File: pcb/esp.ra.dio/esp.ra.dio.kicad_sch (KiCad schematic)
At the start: 26 parts, among them J1 A, J10 UART, J2 B, J3 C, J4 D, J5 START, J6 SELECT, J7 JOY, J8 USB_B_Micro, J9 BATTERY, SW1 RESET, SW2 POWER, SW3 BOOT, U2 VCC, U3 TLV75533PDBV

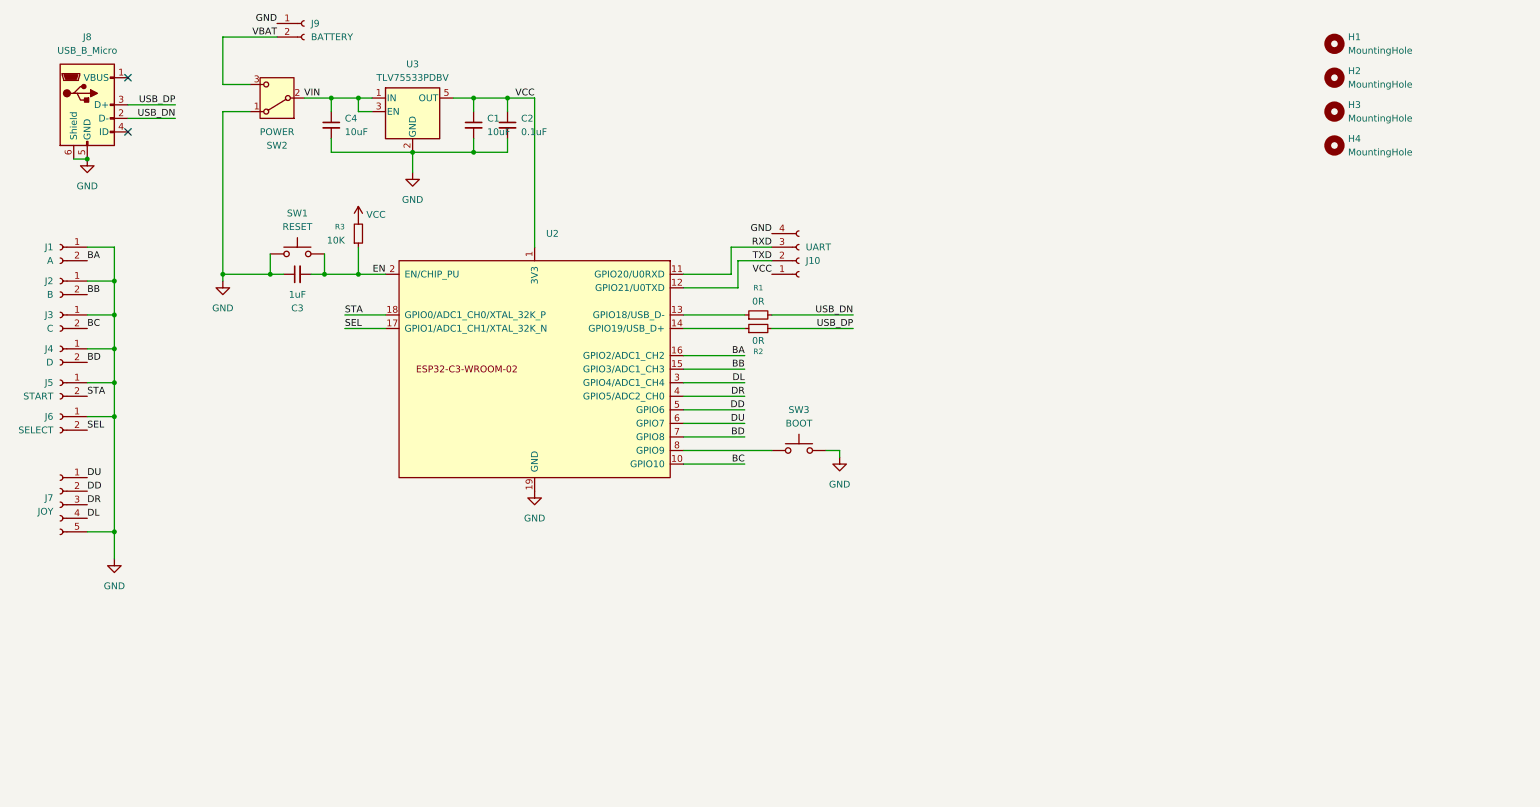
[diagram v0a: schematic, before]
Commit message: Add activity LED, add weak pullups to strapping pins 2 and 8
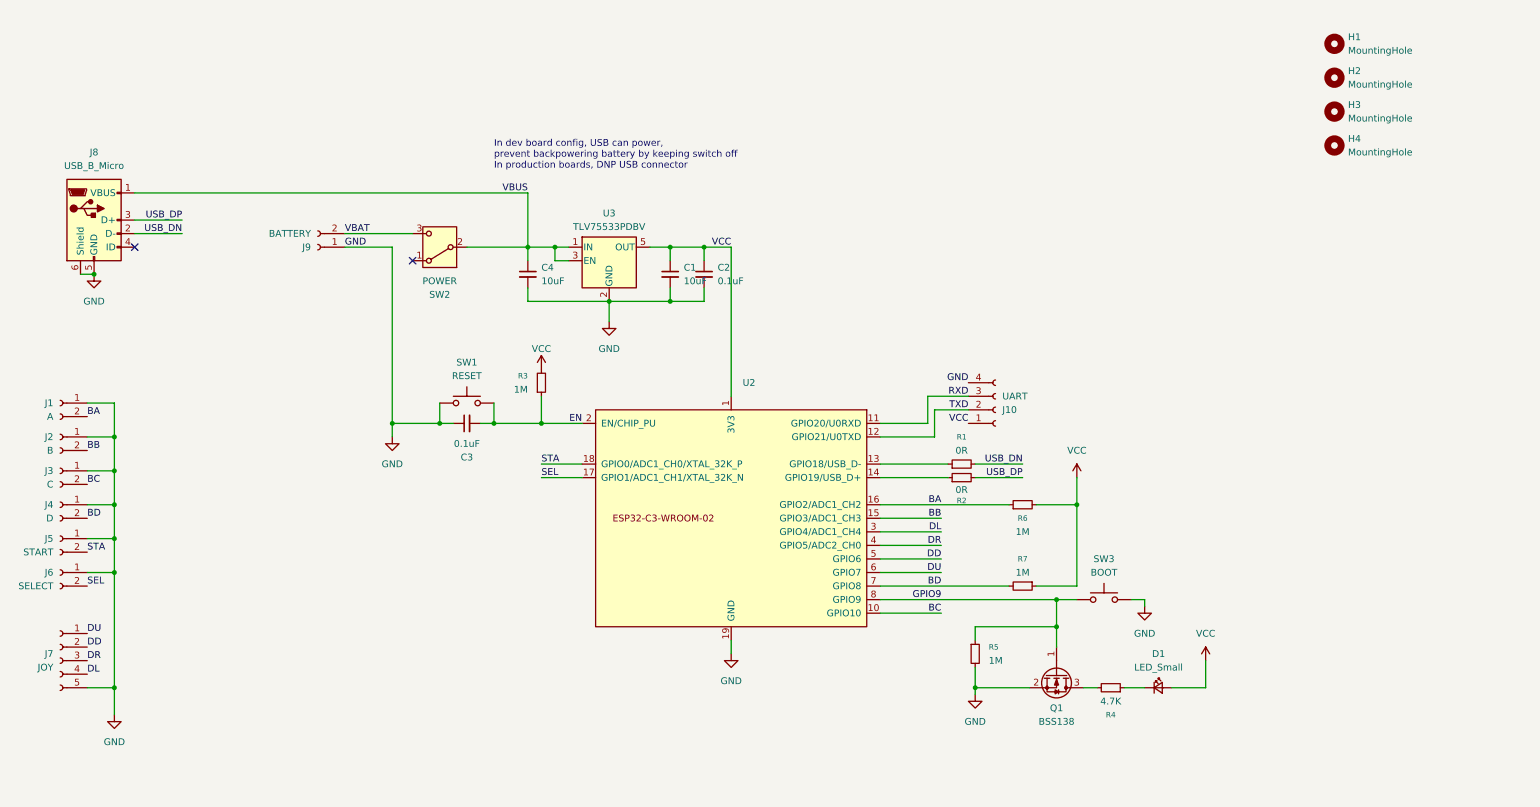
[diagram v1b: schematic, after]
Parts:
- added D1: LED_Small, LED_THT:LED_D3.0mm_Horizontal_O1.27mm_Z6.0mm, symbol Device:LED_Small
- added Q1: BSS138, Package_TO_SOT_SMD:SOT-23, symbol Transistor_FET:BSS138
- added R4: 4.7K, Resistor_SMD:R_0805_2012Metric_Pad1.20x1.40mm_HandSolder, symbol Device:R_Small
- added R5, R6, R7: 1M, Resistor_SMD:R_0805_2012Metric_Pad1.20x1.40mm_HandSolder, symbol Device:R_Small
- C3: value 1uF -> 0.1uF
- R3: value 10K -> 1M
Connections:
- net VIN is gone; now on net VBUS: C4.1, SW2.2 (B), U3.1 (IN), U3.3 (EN)
- net BA: now also R6.1
- net BD: now also R7.2
- net GND: now also Q1.2 (S), R5.2; no longer SW2.1 (A)
- net VCC: now also D1.2 (A), R6.2, R7.1
- net GPIO9: now reaches SW3.1, U2.8 (GPIO9)
- net GPIO9: now also Q1.1 (G), R5.1
- net VBUS: now reaches J8.1 (VBUS)
- new net: D1.1 (K), R4.1
- new net: Q1.3 (D), R4.2
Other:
- note added: "In dev board config, USB can power, prevent backpowering battery by keeping switch off In production boards, DNP USB connector"
- moved on the sheet: C1, C2, C3, C4, J1, J10, J2, J3, J4, J5, J6, J7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

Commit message: Comments and cleanup of routing
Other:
- note removed: "In dev board config, USB can power, prevent backpowering battery by keeping switch off In production boards, DNP USB connector"
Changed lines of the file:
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@@
 		(company "@partlyhuman")
 	)
-	(text "In dev board config, USB can power,\nprevent backpowering battery by keeping switch off\nIn production boards, DNP USB connector"
+	(text_box "USB, RESET, BOOT buttons for development only, can DNP"
 		(exclude_from_sim no)
-		(at 107.95 41.148 0)
+		(at 27.94 30.48 0)
+		(size 26.67 7.62)
+		(margins 0.9525 0.9525 0.9525 0.9525)
+		(stroke
+			(width 0)
+			(type solid)
+		)
+		(fill
+			(type none)
+		)
 		(effects
 			(font
 				(size 1.27 1.27)
 			)
-			(justify left)
+			(justify left top)
 		)
 	)
+	(text_box "GPIO2, GPIO8, GPIO9 used in strapping\nGPIO2, GPIO8 float. GPIO9 has weak int. pullup\nJoint download mode requires\nGPIO2=1 GPIO8=1 GPIO9=0\nR6,R7 pullup GPIO2,8 always\nButton sinks GPIO9 to 0 for boot\nWeak pullups only help the pins' normal common GND button behaviour"
+		(exclude_from_sim no)
+		(at 222.25 91.44 0)
+		(size 50.8 17.78)
+		(margins 0.9525 0.9525 0.9525 0.9525)
+		(stroke
+			(width 0)
+			(type solid)
+		)
+		(fill
+			(type none)
+		)
+		(effects
+			(font
+				(size 1.27 1.27)
+			)
+			(justify left top)
+		)
+	)
+	(text_box "In dev board config, USB can power.\nEngineer must prevent backpowering batt by keeping switch off."
+		(exclude_from_sim no)
+		(at 74.93 30.48 0)
+		(size 39.37 7.62)
+		(margins 0.9525 0.9525 0.9525 0.9525)
+		(stroke
+			(width 0)
+			(type solid)
+		)
+		(fill
+			(type none)
+		)
+		(effects
+			(font
+				(size 1.27 1.27)
+			)
+			(justify left top)
+		)
+	)
+	(text_box "GPIO9 used for LED signalling in production.\nUsing low-side switch to avoid any current leakage.\nShould not interfere with bootstrapping behaviour, normally float with internal pullup to high = normal boot"
+		(exclude_from_sim no)
+		(at 196.85 151.13 0)
+		(size 59.69 10.16)
+		(margins 0.9525 0.9525 0.9525 0.9525)
+		(stroke
+			(width 0)
+			(type solid)
+		)
+		(fill
+			(type none)
+		)
+		(effects
+			(font
+				(size 1.27 1.27)
+			)
+			(justify left top)
+		)
+	)
+	(text_box "UART for programming production units"
+		(exclude_from_sim no)
+		(at 191.77 71.12 0)
+		(size 20.32 7.62)
+		(margins 0.9525 0.9525 0.9525 0.9525)
+		(stroke
+			(width 0)
+			(type solid)
+		)
+		(fill
+			(type none)
+		)
+		(effects
+			(font
+				(size 1.27 1.27)
+			)
+			(justify left top)
+		)
+	)

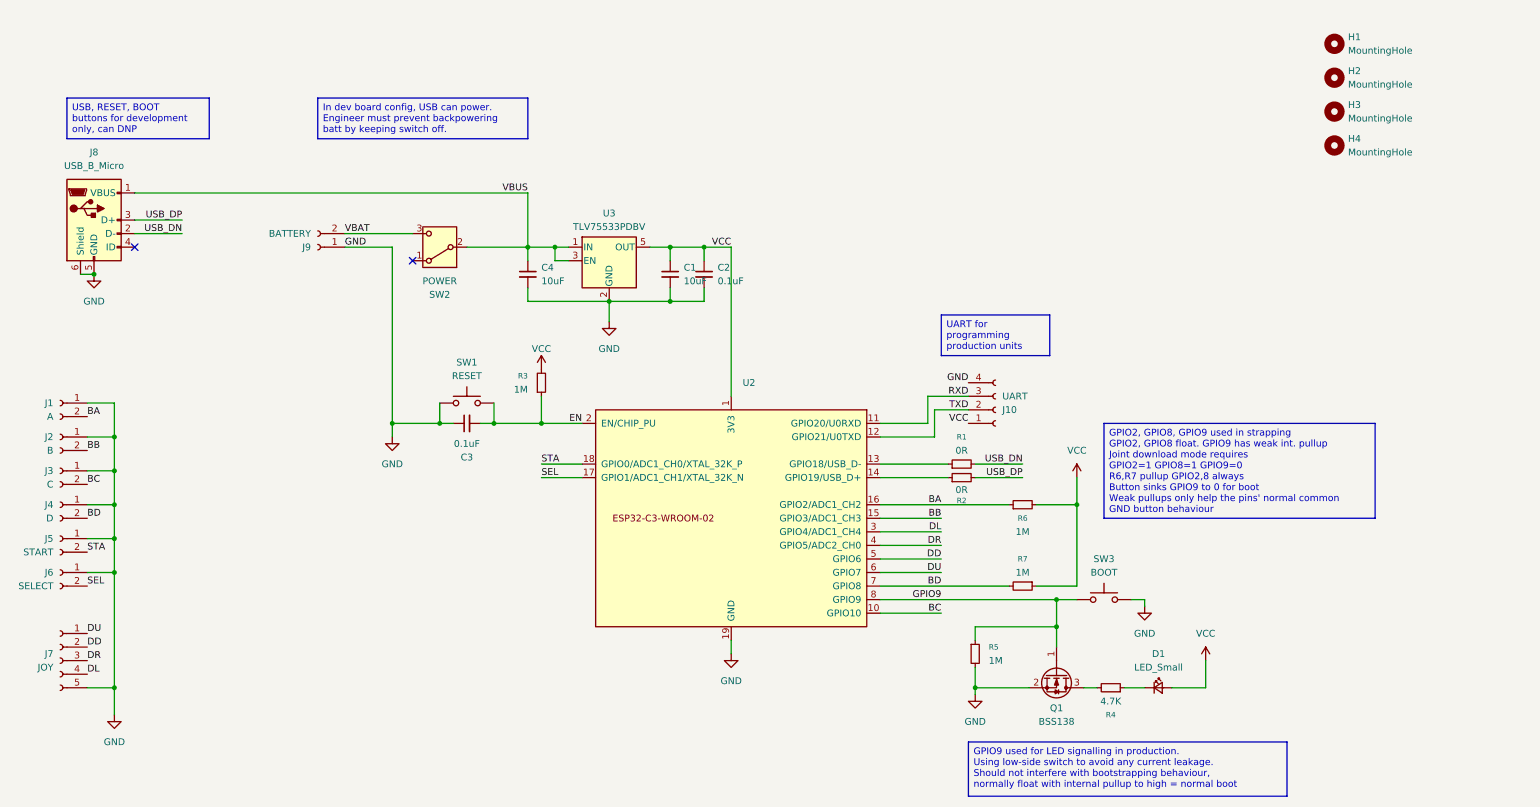
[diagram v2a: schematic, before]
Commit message: Fix strapping pins, move buttons doubling with strapping pins to TX/RX
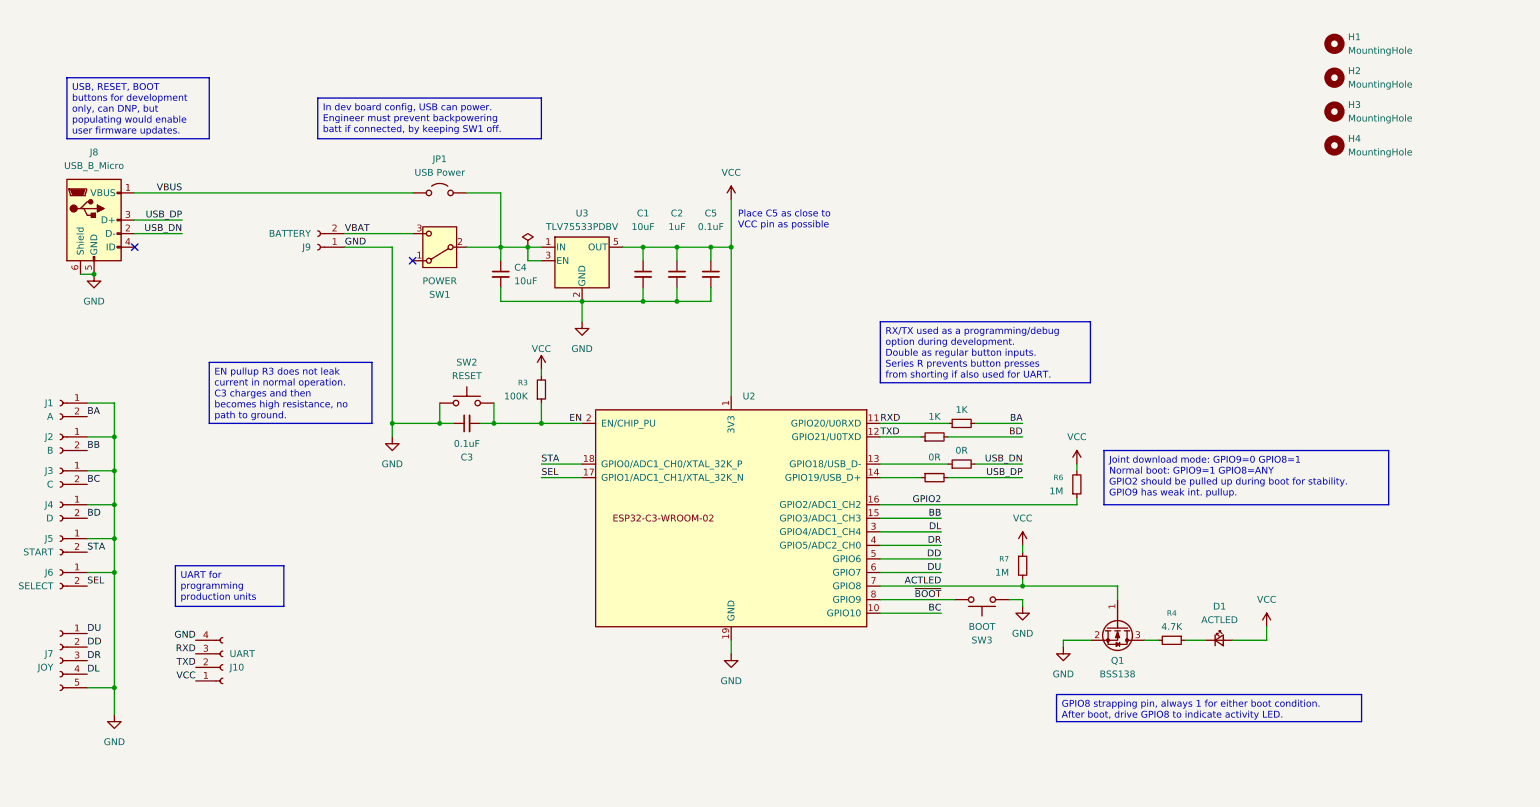
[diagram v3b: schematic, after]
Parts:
- removed R5: 1M, Resistor_SMD:R_0805_2012Metric_Pad1.20x1.40mm_HandSolder, symbol Device:R_Small
- added C5: 0.1uF, Capacitor_SMD:C_0805_2012Metric_Pad1.18x1.45mm_HandSolder, symbol Device:C_Small
- added JP1: USB Power, Connector_PinHeader_2.54mm:PinHeader_1x02_P2.54mm_Vertical, symbol Jumper:Jumper_2_Open
- added R8, R9: 1K, Resistor_SMD:R_0805_2012Metric_Pad1.20x1.40mm_HandSolder, symbol Device:R_Small
- C2: value 0.1uF -> 1uF
- D1: value LED_Small -> ACTLED
- R3: value 1M -> 100K
- renumbered SW2 to SW1, SW1 to SW2
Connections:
- net BA: now also R8.2; no longer R6.1, U2.16 (GPIO2/ADC1_CH2)
- net BD: now also R9.2; no longer R7.2, U2.7 (GPIO8)
- net GND: now also C5.2
- net RXD: now also R8.1
- net TXD: now also R9.1
- net VBUS: now also JP1.1 (A); no longer C4.1, SW1.2 (B), U3.1 (IN), U3.3 (EN)
- net VCC: now also C5.1
- net GPIO9 renamed ~{BOOT}
- net ~{BOOT}: no longer Q1.1 (G)
- new net: C4.1, JP1.2 (B), SW1.2 (B), U3.1 (IN), U3.3 (EN)
- new net ACTLED: Q1.1 (G), R7.2, U2.7 (GPIO8)
- new net GPIO2: R6.1, U2.16 (GPIO2/ADC1_CH2)
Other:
- note added: "Place C5 as close to VCC pin as possible"
- moved on the sheet: C1, C2, C4, D1, J10, Q1, R3, R4, R6, R7, SW3, U3

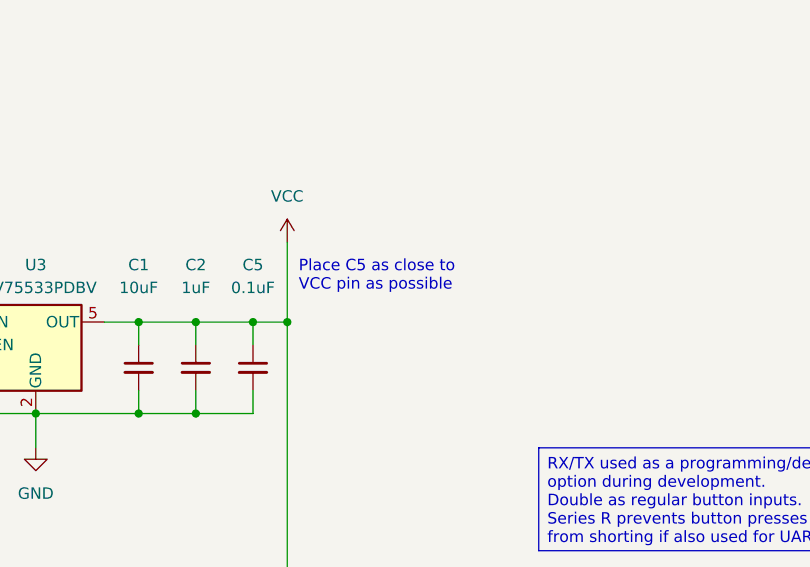
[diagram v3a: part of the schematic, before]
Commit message: oops backwards text
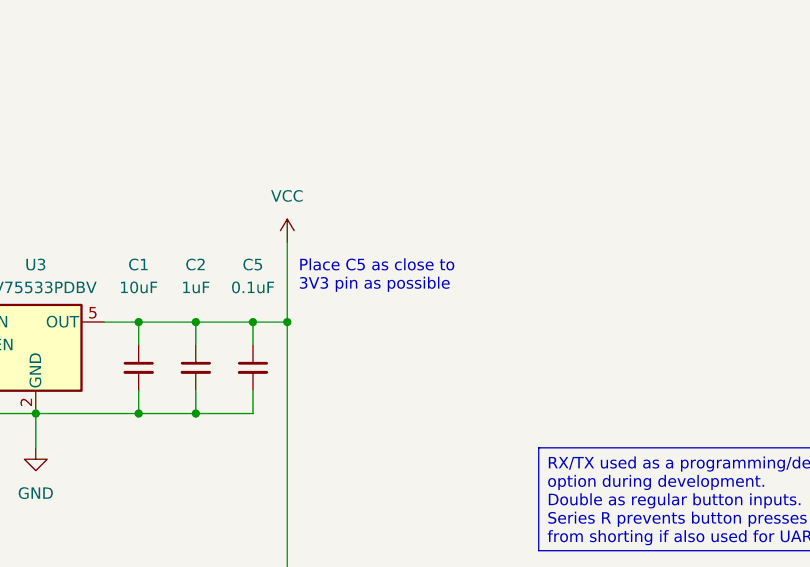
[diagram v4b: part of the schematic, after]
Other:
- note added: "Place C5 as close to 3V3 pin as possible"
- note removed: "Place C5 as close to VCC pin as possible"
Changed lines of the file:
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@@
 		(company "@partlyhuman")
 	)
-	(text "Place C5 as close to\nVCC pin as possible"
+	(text "Place C5 as close to\n3V3 pin as possible"
 		(exclude_from_sim no)
 		(at 153.67 53.34 0)

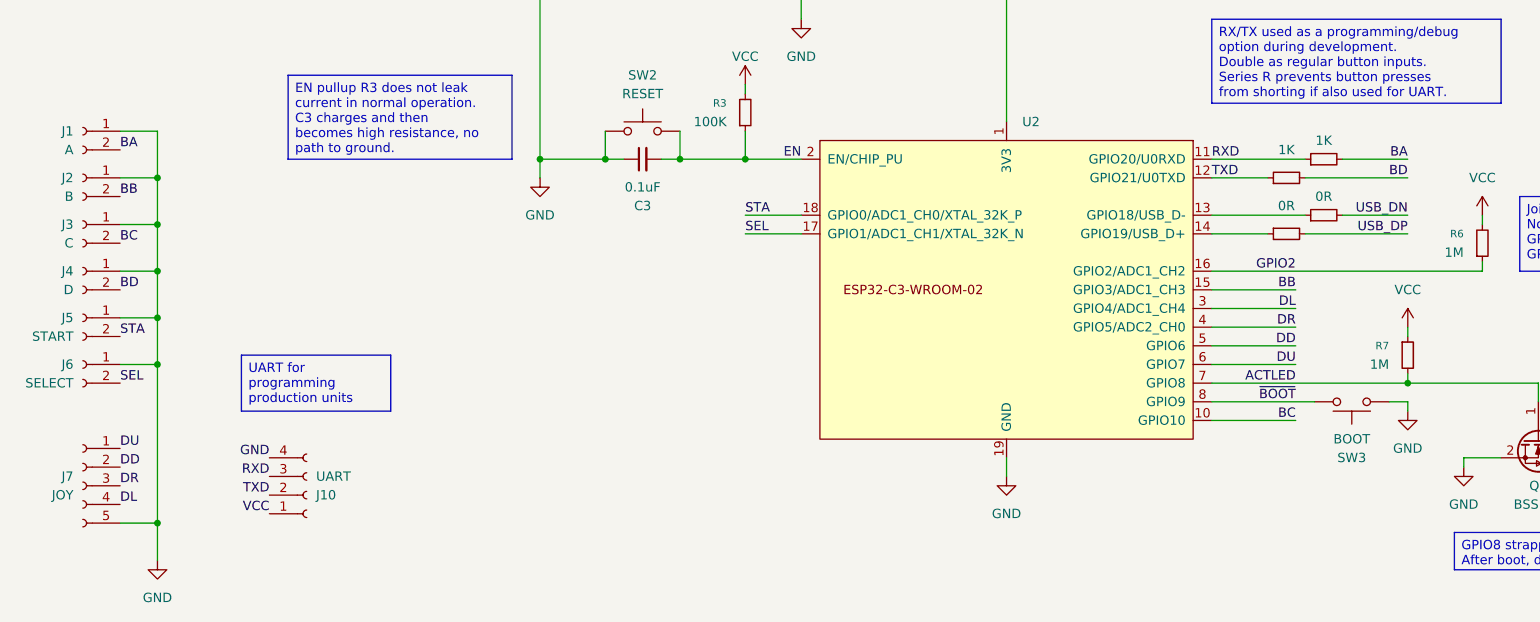
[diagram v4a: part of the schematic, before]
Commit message: PCB rev fixing do-nothing misplaced resistors
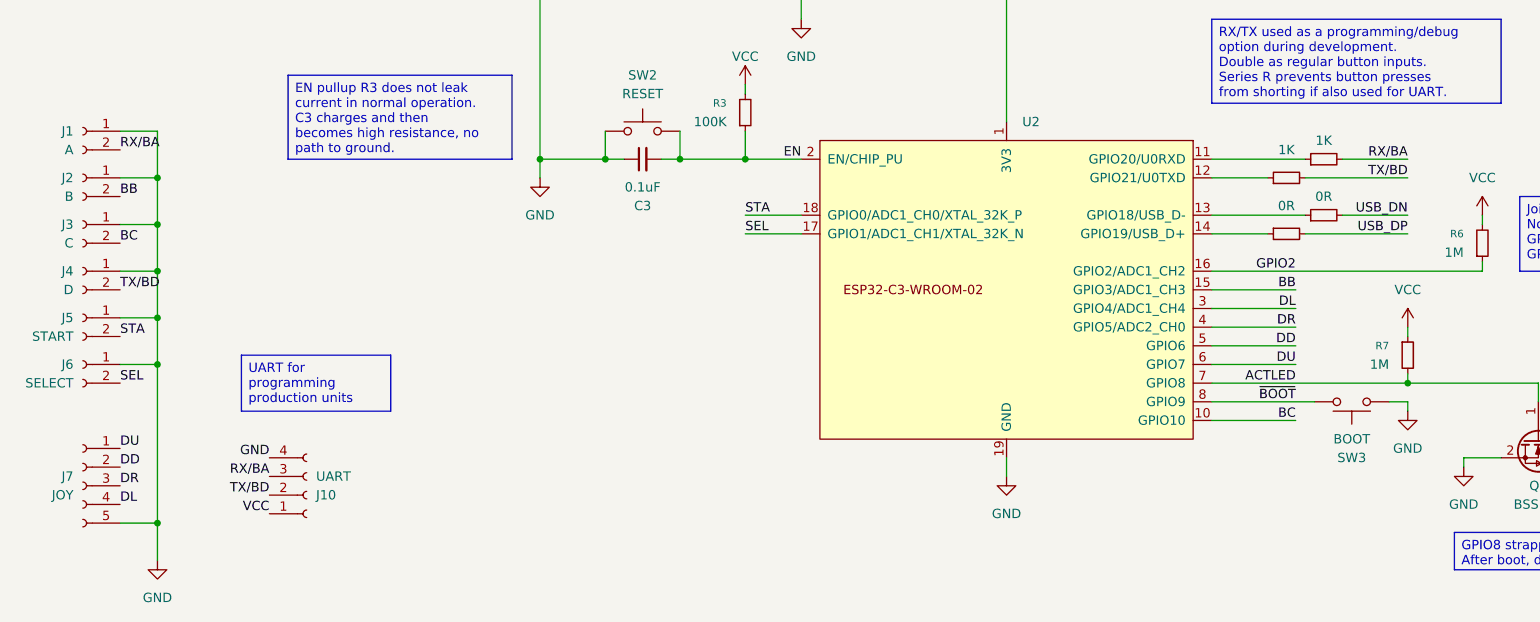
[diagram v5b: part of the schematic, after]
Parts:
- J8: footprint Connector_USB:USB_Micro-AB_Molex_47590-0001 -> Connector_USB:USB_Micro-B_Amphenol_10118193-0002LF_Horizontal
- JP1: footprint Connector_PinHeader_2.54mm:PinHeader_1x02_P2.54mm_Vertical -> Jumper:SolderJumper-2_P1.3mm_Open_TrianglePad1.0x1.5mm
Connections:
- net BA renamed RX/BA
- net RX/BA: now also J10.3 (Pin_3)
- net BD renamed TX/BD
- net TX/BD: now also J10.2 (Pin_2)
- net RXD: no longer names the net of R8.1, U2.11 (GPIO20/U0RXD)
- net RXD: no longer J10.3 (Pin_3)
- net TXD: no longer names the net of R9.1, U2.12 (GPIO21/U0TXD)
- net TXD: no longer J10.2 (Pin_2)

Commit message: IDK
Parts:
- removed R1, R2: 0R, Resistor_SMD:R_0805_2012Metric_Pad1.20x1.40mm_HandSolder, symbol Device:R_Small
- added R10: 1M, Resistor_SMD:R_0805_2012Metric_Pad1.20x1.40mm_HandSolder, symbol Device:R_Small
- U3: value TLV75533PDBV -> RT9080-33GJ5
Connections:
- net ACTLED: now also R10.1
- net GND: now also R10.2
- net USB_DN: now also U2.13 (GPIO18/USB_D-)
- net USB_DP: now also U2.14 (GPIO19/USB_D+)
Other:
- moved on the sheet: R7
